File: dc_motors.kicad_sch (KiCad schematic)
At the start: 18 parts, among them J10 M3_DC, J11 M4_DC, J8 M1_DC, J9 M2_DC, Q2 SIA906EDJ-T1-GE3, Q3 SIA906EDJ-T1-GE3

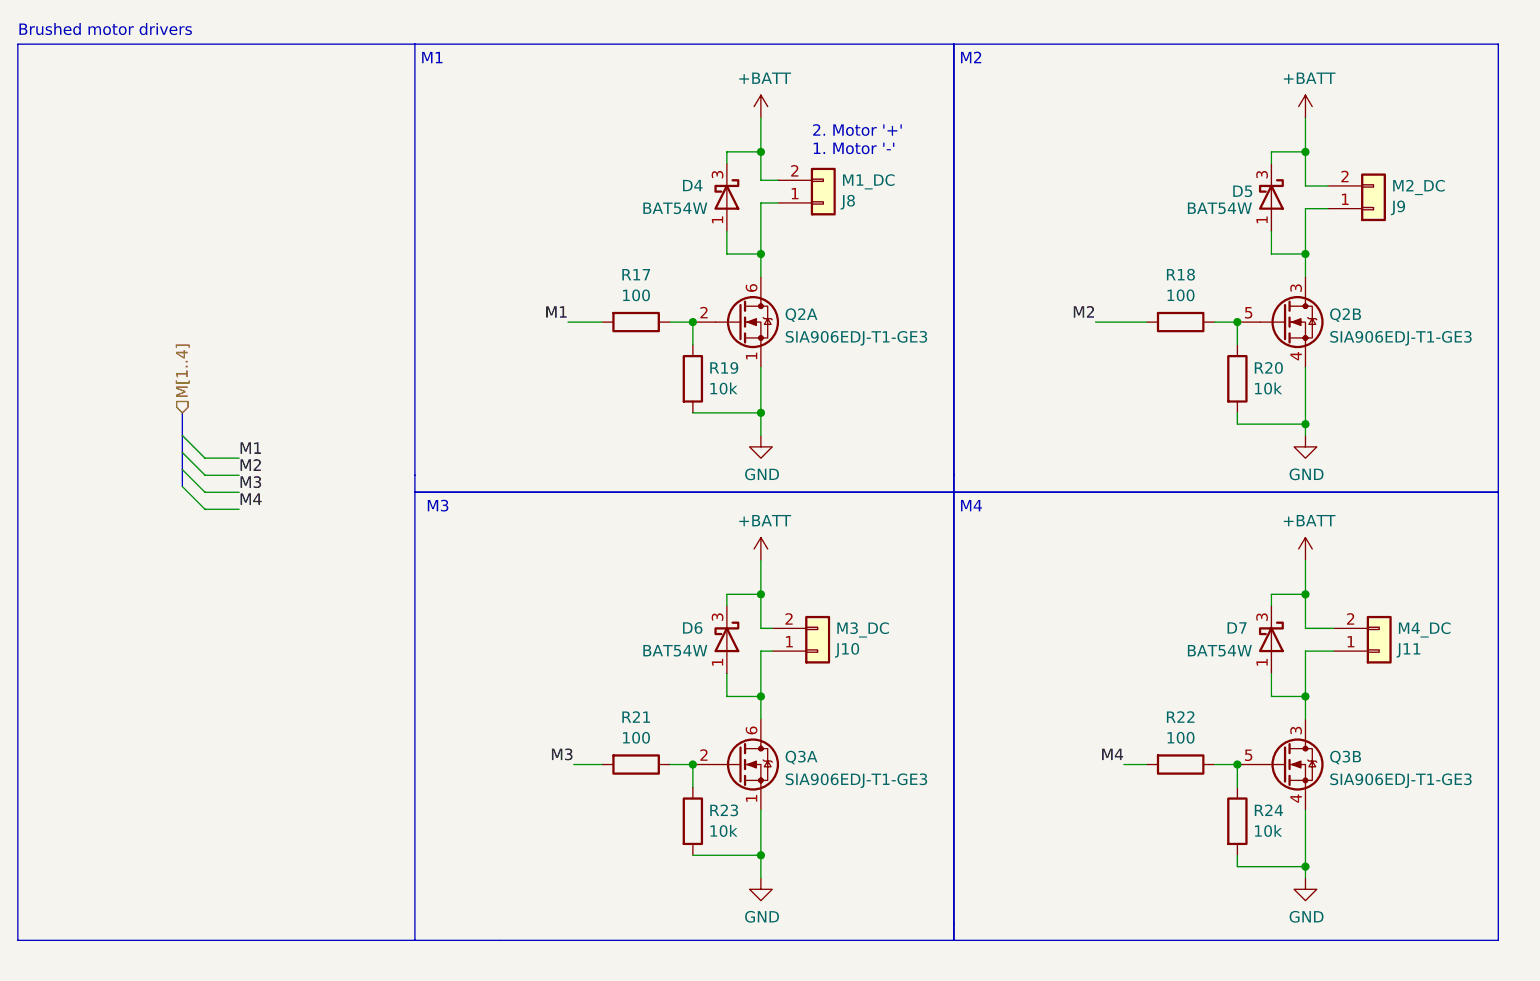
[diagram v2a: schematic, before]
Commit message: fix: Fix D4-D7 schottky mismatch between symbol and footprint
Symbol was placed for diode in SOT-323 package with 3 pins, but
2 pin footprint was assigned. Use generic symbol with two pins.
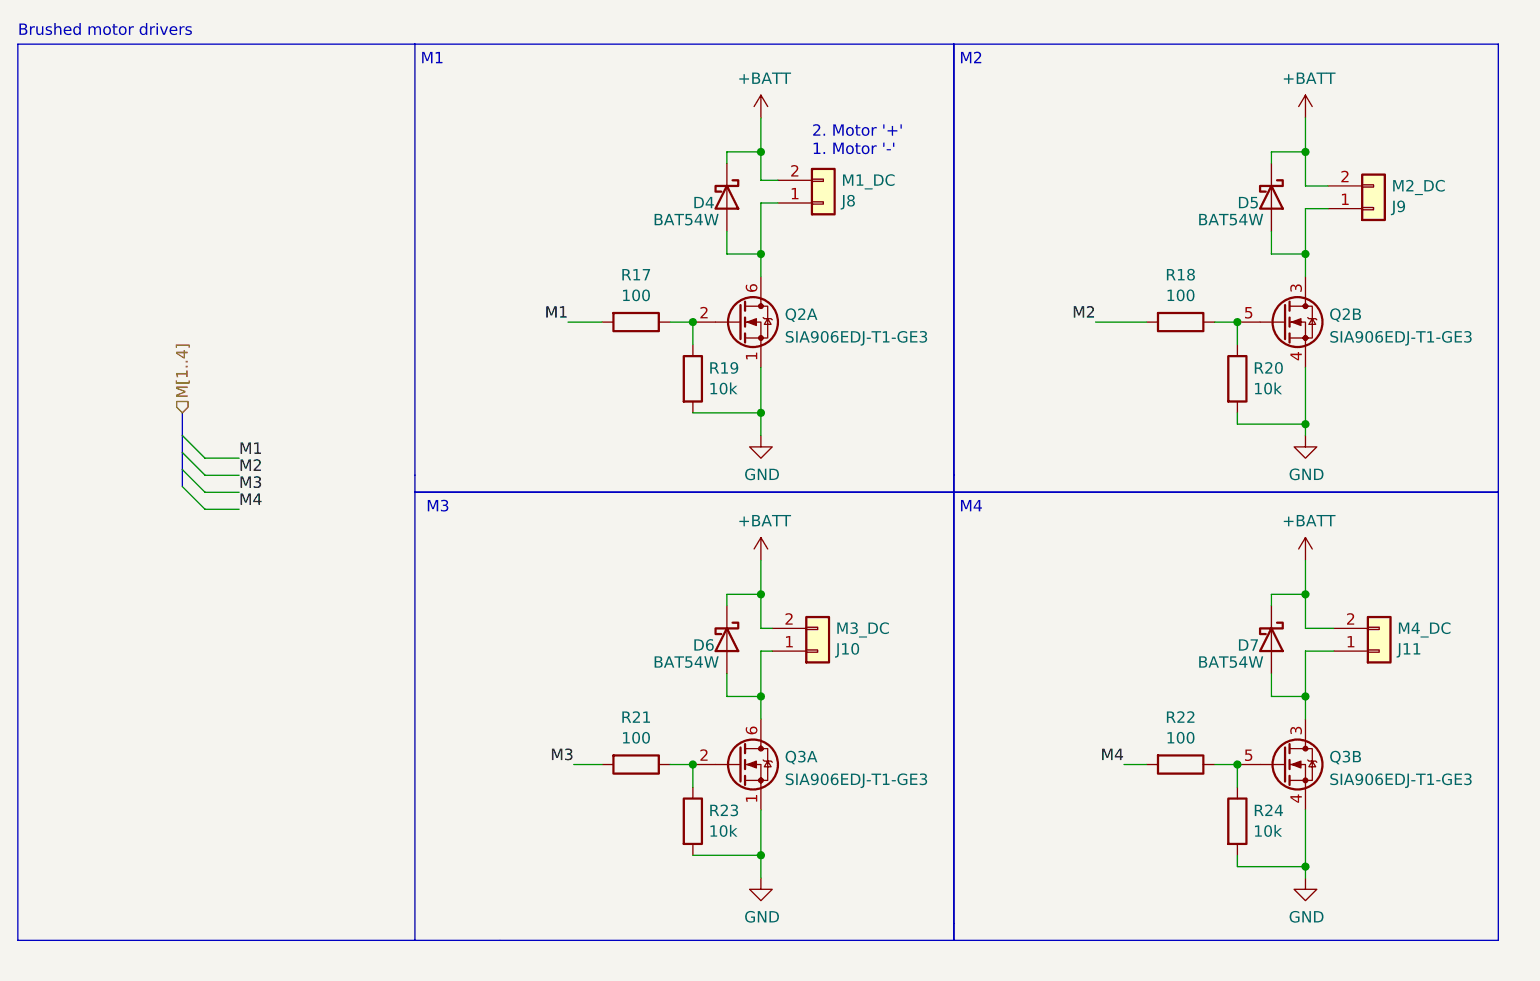
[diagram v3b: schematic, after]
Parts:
- removed D4, D5, D6, D7: BAT54W, Diode_SMD:D_SOD-123, symbol Diode:BAT54W
- added D4, D5, D6, D7: BAT54W, Diode_SMD:D_SOD-123, symbol Device:D_Schottky
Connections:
- net +BATT: now also D4.1 (K), D5.1 (K), D6.1 (K), D7.1 (K)
- net at J9.1 (Pin_1), Q2.3 (D): now also D5.2 (A)
- net at J10.1 (Pin_1), Q3.6 (D): now also D6.2 (A)
- net at J8.1 (Pin_1), Q2.6 (D): now also D4.2 (A)
- net at J11.1 (Pin_1), Q3.3 (D): now also D7.2 (A)
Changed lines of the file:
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@@
+    (pin "2")
+  )
+  (symbol (lib_id "Device:D_Schottky") (at 198.755 59.69 270) (unit 1)
+    (in_bom yes) (on_board yes)
+    (property "Reference" "D5" (id 0) (at 194.945 60.325 90)
+      (effects (font (size 1.27 1.27)) (justify left))
+    )
+    (property "Value" "BAT54W" (id 1) (at 190.5 62.23 90)
+      (effects (font (size 1.27 1.27)) (justify left))
+    )
+    (property "Footprint" "Diode_SMD:D_SOD-123" (id 2) (at 198.755 59.69 0)
+      (effects (font (size 1.27 1.27)) hide)
+    )
+    (property "Datasheet" "~" (id 3) (at 198.755 59.69 0)
+      (effects (font (size 1.27 1.27)) hide)
+    )
+    (property "LCSC" "C915628" (id 4) (at 198.755 59.69 90)
+      (effects (font (size 1.27 1.27)) hide)
+    )
+    (property "JLC" "SOD-123" (id 5) (at 198.755 59.69 90)
+      (effects (font (size 1.27 1.27)) hide)
+    )
+    (pin "1")
+    (pin "2")
+  )
+  (symbol (lib_id "Device:D_Schottky") (at 198.755 109.22 270) (unit 1)
+    (in_bom yes) (on_board yes)
+    (property "Reference" "D7" (id 0) (at 194.945 109.855 90)
+      (effects (font (size 1.27 1.27)) (justify left))
+    )
+    (property "Value" "BAT54W" (id 1) (at 190.5 111.76 90)
+      (effects (font (size 1.27 1.27)) (justify left))
+    )
+    (property "Footprint" "Diode_SMD:D_SOD-123" (id 2) (at 198.755 109.22 0)
+      (effects (font (size 1.27 1.27)) hide)
+    )
+    (property "Datasheet" "~" (id 3) (at 198.755 109.22 0)
+      (effects (font (size 1.27 1.27)) hide)
+    )
+    (property "LCSC" "C915628" (id 4) (at 198.755 109.22 90)
+      (effects (font (size 1.27 1.27)) hide)
+    )
+    (property "JLC" "SOD-123" (id 5) (at 198.755 109.22 90)
+      (effects (font (size 1.27 1.27)) hide)
+    )
+    (pin "1")
     (pin "2")
   )
@@
     (pin "5")
   )
+  (symbol (lib_id "Device:D_Schottky") (at 137.795 109.22 270) (unit 1)
+    (in_bom yes) (on_board yes)
+    (property "Reference" "D6" (id 0) (at 133.985 109.855 90)
+      (effects (font (size 1.27 1.27)) (justify left))
+    )
+    (property "Value" "BAT54W" (id 1) (at 129.54 111.76 90)
+      (effects (font (size 1.27 1.27)) (justify left))
+    )
+    (property "Footprint" "Diode_SMD:D_SOD-123" (id 2) (at 137.795 109.22 0)
+      (effects (font (size 1.27 1.27)) hide)
+    )
+    (property "Datasheet" "~" (id 3) (at 137.795 109.22 0)
+      (effects (font (size 1.27 1.27)) hide)
+    )
+    (property "LCSC" "C915628" (id 4) (at 137.795 109.22 90)
+      (effects (font (size 1.27 1.27)) hide)
+    )
+    (property "JLC" "SOD-123" (id 5) (at 137.795 109.22 90)
+      (effects (font (size 1.27 1.27)) hide)
+    )
+    (pin "1")
+    (pin "2")
+  )
   (symbol (lib_id "Device:Q_Dual_NMOS_S1G1D2S2G2D1") (at 139.065 123.19 0) (unit 1)
     (in_bom yes) (on_board yes) (fields_autoplaced)
@@
     (pin "2")
   )
-  (symbol (lib_id "Diode:BAT54W") (at 198.755 59.69 270) (unit 1)
-    (in_bom yes) (on_board yes)
-    (property "Reference" "D5" (id 0) (at 194.31 59.055 90)
-      (effects (font (size 1.27 1.27)) (justify left))
-    )
-    (property "Value" "BAT54W" (id 1) (at 189.23 60.96 90)
-      (effects (font (size 1.27 1.27)) (justify left))
-    )
-    (property "Footprint" "Diode_SMD:D_SOD-123" (id 2) (at 194.31 59.69 0)
-      (effects (font (size 1.27 1.27)) hide)
-    )
-    (property "Datasheet" "https://assets.nexperia.com/documents/data-sheet/BAT54W_SER.pdf" (id 3) (at 198.755 59.69 0)
-      (effects (font (size 1.27 1.27)) hide)
-    )
-    (property "JLC" "SOD-123" (id 4) (at 198.755 59.69 0)
-      (effects (font (size 1.27 1.27)) hide)
-    )
-    (property "LCSC" "C915628" (id 5) (at 198.755 59.69 0)
-      (effects (font (size 1.27 1.27)) hide)
-    )
-    (pin "1")
-    (pin "2")
-    (pin "3")
-  )
-  (symbol (lib_id "Diode:BAT54W") (at 137.795 59.69 270) (unit 1)
-    (in_bom yes) (on_board yes)
-    (property "Reference" "D4" (id 0) (at 132.715 58.42 90)
-      (effects (font (size 1.27 1.27)) (justify left))
-    )
-    (property "Value" "BAT54W" (id 1) (at 128.27 60.96 90)
-      (effects (font (size 1.27 1.27)) (justify left))
-    )
-    (property "Footprint" "Diode_SMD:D_SOD-123" (id 2) (at 133.35 59.69 0)
-      (effects (font (size 1.27 1.27)) hide)
-    )
-    (property "Datasheet" "https://assets.nexperia.com/documents/data-sheet/BAT54W_SER.pdf" (id 3) (at 137.795 59.69 0)
-      (effects (font (size 1.27 1.27)) hide)
-    )
-    (property "JLC" "SOD-123" (id 4) (at 137.795 59.69 0)
-      (effects (font (size 1.27 1.27)) hide)
-    )
-    (property "LCSC" "C915628" (id 5) (at 137.795 59.69 0)
-      (effects (font (size 1.27 1.27)) hide)
-    )
-    (pin "1")
-    (pin "2")
-    (pin "3")
-  )
-  (symbol (lib_id "Diode:BAT54W") (at 198.755 109.22 270) (unit 1)
-    (in_bom yes) (on_board yes)
-    (property "Reference" "D7" (id 0) (at 193.675 107.95 90)
-      (effects (font (size 1.27 1.27)) (justify left))
-    )
-    (property "Value" "BAT54W" (id 1) (at 189.23 110.49 90)
-      (effects (font (size 1.27 1.27)) (justify left))
-    )
-    (property "Footprint" "Diode_SMD:D_SOD-123" (id 2) (at 194.31 109.22 0)
-      (effects (font (size 1.27 1.27)) hide)
-    )
-    (property "Datasheet" "https://assets.nexperia.com/documents/data-sheet/BAT54W_SER.pdf" (id 3) (at 198.755 109.22 0)
-      (effects (font (size 1.27 1.27)) hide)
-    )
-    (property "JLC" "SOD-123" (id 4) (at 198.755 109.22 0)
-      (effects (font (size 1.27 1.27)) hide)
-    )
-    (property "LCSC" "C915628" (id 5) (at 198.755 109.22 0)
-      (effects (font (size 1.27 1.27)) hide)
-    )
-    (pin "1")
-    (pin "2")
-    (pin "3")
+  (symbol (lib_id "Device:D_Schottky") (at 137.795 59.69 270) (unit 1)
+    (in_bom yes) (on_board yes)
+    (property "Reference" "D4" (id 0) (at 133.985 60.325 90)
+      (effects (font (size 1.27 1.27)) (justify left))
+    )
+    (property "Value" "BAT54W" (id 1) (at 129.54 62.23 90)
+      (effects (font (size 1.27 1.27)) (justify left))
+    )
+    (property "Footprint" "Diode_SMD:D_SOD-123" (id 2) (at 137.795 59.69 0)
+      (effects (font (size 1.27 1.27)) hide)
+    )
+    (property "Datasheet" "~" (id 3) (at 137.795 59.69 0)
+      (effects (font (size 1.27 1.27)) hide)
+    )
+    (property "LCSC" "C915628" (id 4) (at 137.795 59.69 90)
+      (effects (font (size 1.27 1.27)) hide)
+    )
+    (property "JLC" "SOD-123" (id 5) (at 137.795 59.69 90)
+      (effects (font (size 1.27 1.27)) hide)
+    )
+    (pin "1")
+    (pin "2")
   )
   (symbol (lib_id "Device:Q_Dual_NMOS_S1G1D2S2G2D1") (at 139.065 73.66 0) (unit 1)
@@
     (pin "2")
   )
-  (symbol (lib_id "Diode:BAT54W") (at 137.795 109.22 270) (unit 1)
-    (in_bom yes) (on_board yes)
-    (property "Reference" "D6" (id 0) (at 132.715 107.95 90)
-      (effects (font (size 1.27 1.27)) (justify left))
-    )
-    (property "Value" "BAT54W" (id 1) (at 128.27 110.49 90)
-      (effects (font (size 1.27 1.27)) (justify left))
-    )
-    (property "Footprint" "Diode_SMD:D_SOD-123" (id 2) (at 133.35 109.22 0)
-      (effects (font (size 1.27 1.27)) hide)
-    )
-    (property "Datasheet" "https://assets.nexperia.com/documents/data-sheet/BAT54W_SER.pdf" (id 3) (at 137.795 109.22 0)
-      (effects (font (size 1.27 1.27)) hide)
-    )
-    (property "JLC" "SOD-123" (id 4) (at 137.795 109.22 0)
-      (effects (font (size 1.27 1.27)) hide)
-    )
-    (property "LCSC" "C915628" (id 5) (at 137.795 109.22 0)
-      (effects (font (size 1.27 1.27)) hide)
-    )
-    (pin "1")
-    (pin "2")
-    (pin "3")
-  )
   (symbol (lib_id "Connector_Generic:Conn_01x02") (at 210.185 60.96 0) (mirror x) (unit 1)
